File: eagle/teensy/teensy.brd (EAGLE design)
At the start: 38.1 x 35.6 mm, 8 parts

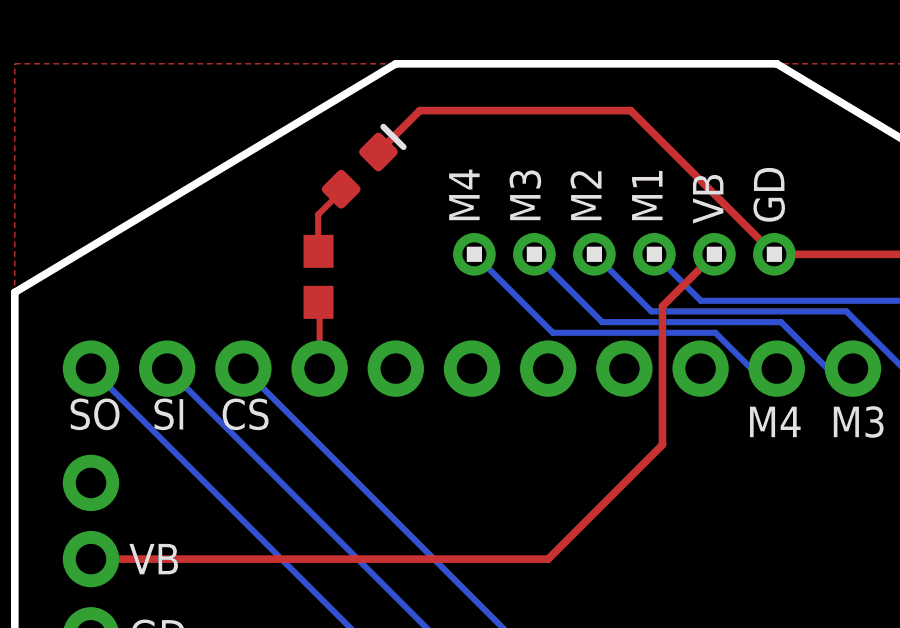
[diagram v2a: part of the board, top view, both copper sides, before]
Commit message: modified:   eagle/teensy/teensy.brd
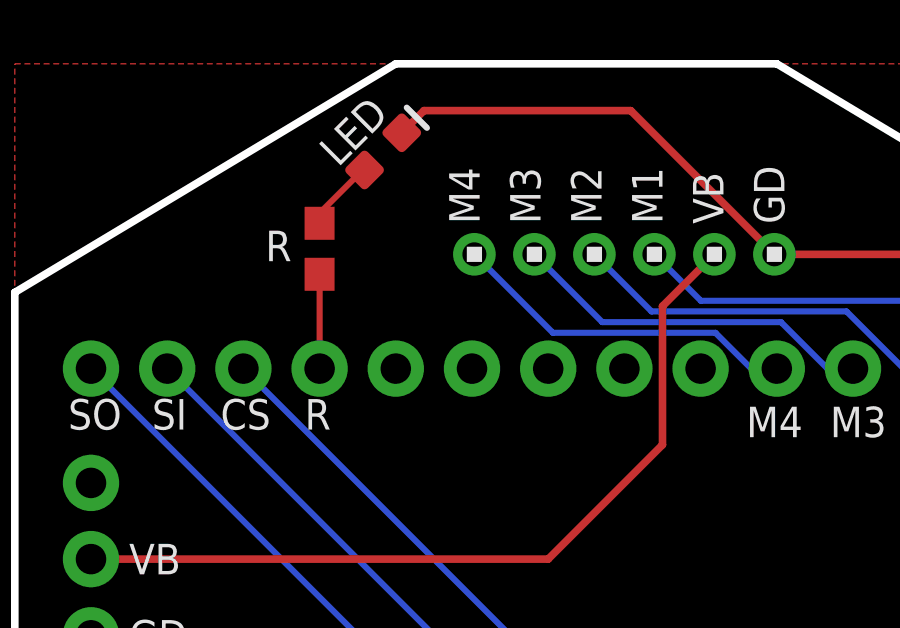
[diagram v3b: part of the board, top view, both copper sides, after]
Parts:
- moved D1 1.01 mm to (12.3, 32.6)
- moved R1 0.94 mm to (10.2, 29.4)
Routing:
- net GND: track 83.8 -> 82.8 mm
- net R1: track 2.22 -> 3.14 mm
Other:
- board text added: "LED"
- board text added: "R"
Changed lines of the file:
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@@
 <text x="17.526" y="0.762" size="0.8128" layer="25">5V</text>
 <text x="19.304" y="0.762" size="0.8128" layer="25">SBUS</text>
+<text x="8.35611875" y="28.98153125" size="1.016" layer="25">R</text>
+<text x="10.77499375" y="32.08946875" size="1.016" layer="25" rot="R45">LED</text>
+<text x="9.6640625" y="23.368" size="1.016" layer="25">R</text>
 </plain>
 <attributes>
@@
 <attribute name="VALUE" x="1.27" y="8.128" size="0.6096" layer="27" font="vector" ratio="20"/>
 </element>
-<element name="D1" library="SparkFun-LED" package="LED-0603" value="WHITE" x="11.5" y="32" smashed="yes" rot="R45">
-<attribute name="PROD_ID" value="DIO-09004" x="11.5" y="32" size="1.778" layer="27" rot="R45" display="off"/>
-</element>
-<element name="R1" library="SparkFun-Resistors" package="0603" value="22" x="10.12456875" y="28.458459375" smashed="yes" rot="R90">
-<attribute name="PROD_ID" value="RES-08698" x="10.12456875" y="28.458459375" size="1.778" layer="27" rot="R90" display="off"/>
+<element name="D1" library="SparkFun-LED" package="LED-0603" value="WHITE" x="12.278584375" y="32.640265625" smashed="yes" rot="R45">
+<attribute name="PROD_ID" value="DIO-09004" x="12.278584375" y="32.640265625" size="1.778" layer="27" rot="R45" display="off"/>
+</element>
+<element name="R1" library="SparkFun-Resistors" package="0603" value="22" x="10.159171875" y="29.3929" smashed="yes" rot="R90">
+<attribute name="PROD_ID" value="RES-08698" x="10.159171875" y="29.3929" size="1.778" layer="27" rot="R90" display="off"/>
 </element>
 </elements>
@@
 <contactref element="D1" pad="C"/>
 <wire x1="25.32" y1="29.21" x2="20.53" y2="34" width="0.254" layer="1"/>
-<wire x1="20.53" y1="34" x2="13.5" y2="34" width="0.254" layer="1"/>
-<wire x1="13.5" y1="34" x2="12.12013125" y2="32.62013125" width="0.254" layer="1"/>
+<wire x1="20.53" y1="34" x2="13.63831875" y2="34" width="0.254" layer="1"/>
+<wire x1="13.63831875" y1="34" x2="12.898715625" y2="33.260396875" width="0.254" layer="1"/>
 </signal>
 <signal name="5V">
@@
 <contactref element="D1" pad="A"/>
 <contactref element="R1" pad="2"/>
-<wire x1="10.879865625" y1="31.379865625" x2="10.879865625" y2="31.300015625" width="0.2032" layer="1"/>
-<wire x1="10.879865625" y1="31.300015625" x2="10.113484375" y2="30.533634375" width="0.2032" layer="1"/>
-<wire x1="10.113484375" y1="30.533634375" x2="10.113484375" y2="29.31954375" width="0.2032" layer="1"/>
-<wire x1="10.113484375" y1="29.31954375" x2="10.12456875" y2="29.308459375" width="0.2032" layer="1"/>
+<wire x1="11.65845" y1="32.02013125" x2="11.59998125" y2="32.02013125" width="0.2032" layer="1"/>
+<wire x1="11.59998125" y1="32.02013125" x2="10.113484375" y2="30.533634375" width="0.2032" layer="1"/>
+<wire x1="10.113484375" y1="30.533634375" x2="10.113484375" y2="30.2885875" width="0.2032" layer="1"/>
+<wire x1="10.113484375" y1="30.2885875" x2="10.159171875" y2="30.2429" width="0.2032" layer="1"/>
 </signal>
 <signal name="R1">
 <contactref element="R1" pad="1"/>
 <contactref element="J2" pad="4"/>
-<wire x1="10.16" y1="25.4" x2="10.16" y2="27.573028125" width="0.2032" layer="1"/>
-<wire x1="10.16" y1="27.573028125" x2="10.12456875" y2="27.608459375" width="0.2032" layer="1"/>
+<wire x1="10.16" y1="25.4" x2="10.16" y2="28.542071875" width="0.2032" layer="1"/>
+<wire x1="10.16" y1="28.542071875" x2="10.159171875" y2="28.5429" width="0.2032" layer="1"/>
 </signal>
 </signals>
